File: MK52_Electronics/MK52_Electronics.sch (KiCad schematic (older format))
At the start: 21 parts, among them J1 Processor, J2 KBD Columns, J3 KBD Rows, Q1 BS250, Q2 2N7000, Q3 2N7000, SW1 POWER, U1 4040, U2 4051, U3 4051

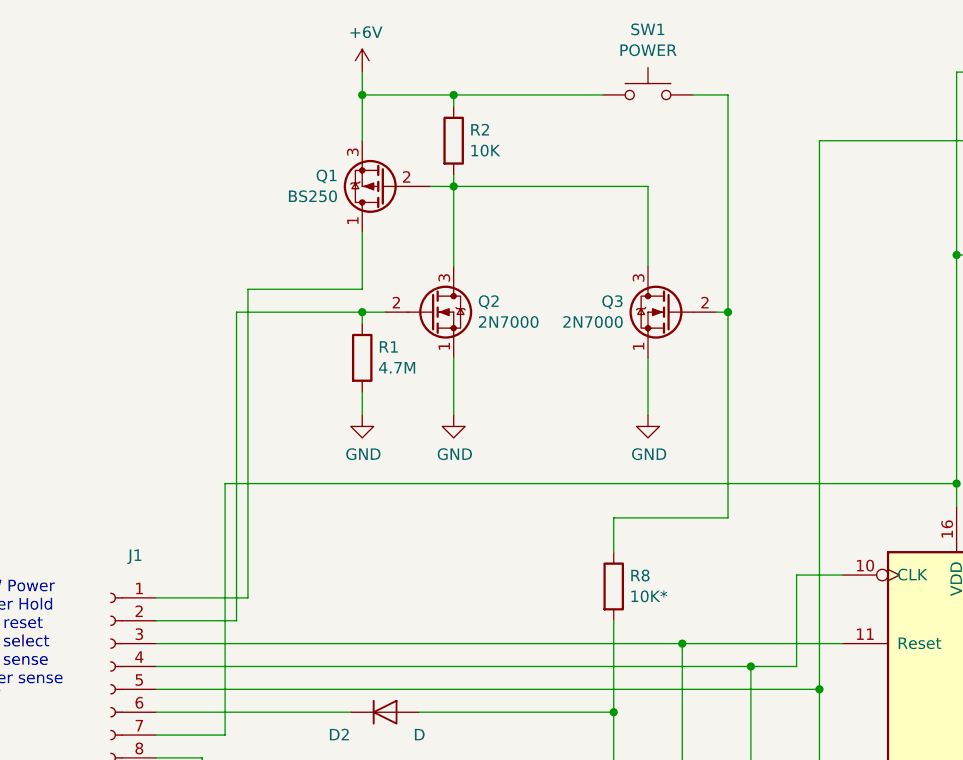
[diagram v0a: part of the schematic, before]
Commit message: Updated gate resistors
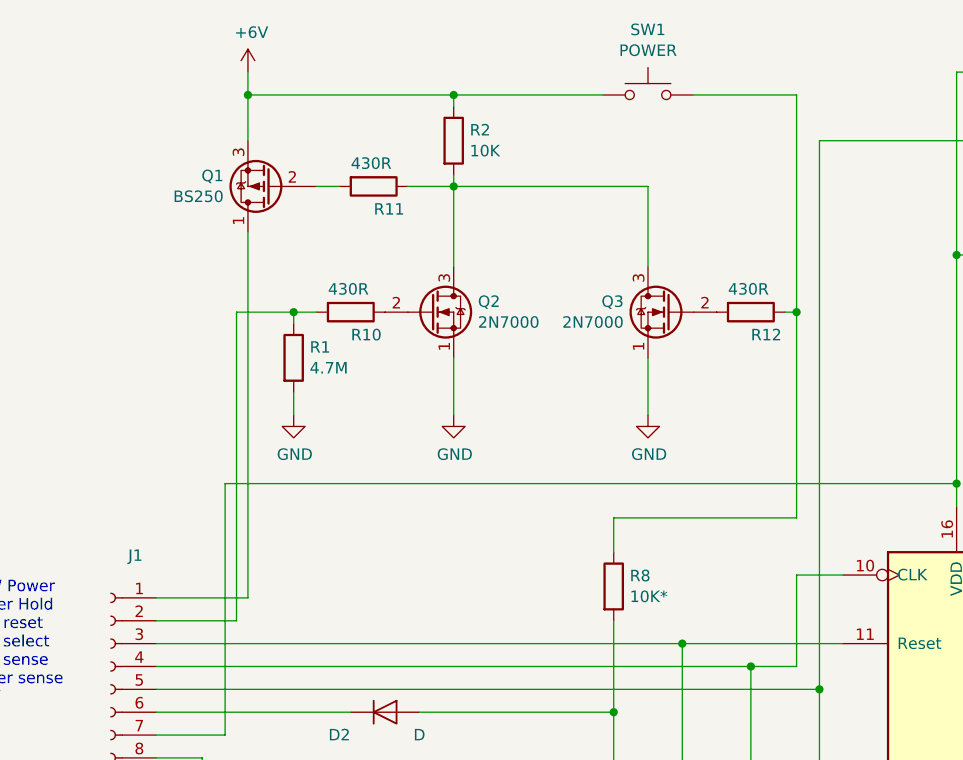
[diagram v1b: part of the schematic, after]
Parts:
- added R10, R11, R12: 430R, symbol Device:R
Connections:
- net at Q2.3 (D), Q3.3 (D), R2.2: now also R11.1; no longer Q1.2 (G)
- net at J1.2 (Pin_2), R1.1: now also R10.2; no longer Q2.2 (G)
- net at R8.1, SW1.2: now also R12.1; no longer Q3.2 (G)
- new net: Q1.2 (G), R11.2
- new net: Q2.2 (G), R10.1
- new net: Q3.2 (G), R12.2
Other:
- moved on the sheet: Q1, R1
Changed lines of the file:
@@
 EESchema Schematic File Version 4
+LIBS:MK52_Electronics-cache
 EELAYER 29 0
 EELAYER END
@@
 L Transistor_FET:BS250 Q1
 U 1 1 5FE6E4D4
-P 3900 1300
-F 0 "Q1" H 4106 1254 50  0000 L CNN
-F 1 "BS250" H 4106 1345 50  0000 L CNN
-F 2 "Package_TO_SOT_THT:TO-92_Inline" H 4100 1225 50  0001 L CIN
-F 3 "http://www.vishay.com/docs/70209/70209.pdf" H 3900 1300 50  0001 L CNN
-	1    3900 1300
+P 3400 1300
+F 0 "Q1" H 3606 1254 50  0000 L CNN
+F 1 "BS250" H 3606 1345 50  0000 L CNN
+F 2 "Package_TO_SOT_THT:TO-92_Inline" H 3600 1225 50  0001 L CIN
+F 3 "http://www.vishay.com/docs/70209/70209.pdf" H 3400 1300 50  0001 L CNN
+	1    3400 1300
 	-1   0    0    1
 $EndComp
@@
 L power:+6V #PWR02
 U 1 1 5FE6EF69
-P 3800 800
-F 0 "#PWR02" H 3800 650 50  0001 C CNN
-F 1 "+6V" H 3815 973 50  0000 C CNN
-F 2 "" H 3800 800 50  0001 C CNN
-F 3 "" H 3800 800 50  0001 C CNN
-	1    3800 800
-	1    0    0    -1
-$EndComp
-Wire Wire Line
-	3800 800  3800 900
+P 3300 800
+F 0 "#PWR02" H 3300 650 50  0001 C CNN
+F 1 "+6V" H 3315 973 50  0000 C CNN
+F 2 "" H 3300 800 50  0001 C CNN
+F 3 "" H 3300 800 50  0001 C CNN
+	1    3300 800
+	1    0    0    -1
+$EndComp
 $Comp
 L Device:R R2
@@
 $EndComp
 Wire Wire Line
-	4100 1300 4200 1300
-Wire Wire Line
 	4200 1300 4200 1250
 Wire Wire Line
-	3800 900  4200 900
-Wire Wire Line
 	4200 900  4200 950
-Connection ~ 3800 900
-Wire Wire Line
-	3800 900  3800 1100
-Wire Wire Line
-	3800 1750 3800 1500
 Text Notes 1950 3650 0    50   ~ 0
 1 - RAW Power\n2 - Power Hold\n3 - KBD reset\n4 - KBD select\n5 - KBD sense\n6 - Power sense\n7 - 3.3V\n8 - GND
@@
 L Device:R R1
 U 1 1 5FE77DA3
-P 3800 2050
-F 0 "R1" H 3870 2096 50  0000 L CNN
-F 1 "4.7M" H 3870 2005 50  0000 L CNN
-F 2 "" V 3730 2050 50  0001 C CNN
-F 3 "~" H 3800 2050 50  0001 C CNN
-	1    3800 2050
+P 3500 2050
+F 0 "R1" H 3570 2096 50  0000 L CNN
+F 1 "4.7M" H 3570 2005 50  0000 L CNN
+F 2 "" V 3430 2050 50  0001 C CNN
+F 3 "~" H 3500 2050 50  0001 C CNN
+	1    3500 2050
 	1    0    0    -1
 $EndComp
 Wire Wire Line
 	4200 1300 4200 1650
-Wire Wire Line
-	3300 1750 3800 1750
 $Comp
 L power:GND #PWR06
@@
 	1    0    0    -1
 $EndComp
-Wire Wire Line
-	3250 1850 3800 1850
 $Comp
 L power:GND #PWR03
 U 1 1 5FE8927B
-P 3800 2300
-F 0 "#PWR03" H 3800 2050 50  0001 C CNN
-F 1 "GND" H 3805 2127 50  0000 C CNN
-F 2 "" H 3800 2300 50  0001 C CNN
-F 3 "" H 3800 2300 50  0001 C CNN
-	1    3800 2300
+P 3500 2300
+F 0 "#PWR03" H 3500 2050 50  0001 C CNN
+F 1 "GND" H 3505 2127 50  0000 C CNN
+F 2 "" H 3500 2300 50  0001 C CNN
+F 3 "" H 3500 2300 50  0001 C CNN
+	1    3500 2300
 	1    0    0    -1
 $EndComp
 Wire Wire Line
 	4200 2050 4200 2300
-Wire Wire Line
-	3800 2200 3800 2300
-Wire Wire Line
-	3800 1850 3800 1900
-Connection ~ 3800 1850
-Wire Wire Line
-	3800 1850 3900 1850
 $Comp
 L Transistor_FET:2N7000 Q3
@@
 	2900 3100 3300 3100
 Wire Wire Line
-	3300 1750 3300 3100
-Wire Wire Line
 	2900 3200 3250 3200
 Wire Wire Line
@@
 Wire Wire Line
 	2900 3600 3750 3600
-Wire Wire Line
-	5400 2750 5400 1850
-Wire Wire Line
-	5400 1850 5350 1850
 $Comp
 L Switch:SW_Push SW1
@@
 	1    0    0    -1
 $EndComp
-Connection ~ 5400 1850
 Wire Wire Line
 	4900 4150 4900 4300
@@
 Wire Wire Line
 	4900 2900 4900 2750
-Wire Wire Line
-	4900 2750 5400 2750
 Connection ~ 4900 3600
 Wire Wire Line
@@
 Connection ~ 4200 900
 Wire Wire Line
-	5250 900  5400 900
-Wire Wire Line
-	5400 900  5400 1850
-Wire Wire Line
 	6400 800  6400 1600
 Wire Wire Line
@@
 Wire Wire Line
 	6400 800  8500 800
+$Comp
+L Device:R R11
+U 1 1 6003BE54
+P 3850 1300
+F 0 "R11" V 3950 1300 50  0000 L CNN
+F 1 "430R" V 3750 1200 50  0000 L CNN
+F 2 "" V 3780 1300 50  0001 C CNN
+F 3 "~" H 3850 1300 50  0001 C CNN
+	1    3850 1300
+	0    1    1    0
+$EndComp
+Wire Wire Line
+	3600 1300 3700 1300
+Wire Wire Line
+	4000 1300 4200 1300
+Wire Wire Line
+	3300 1100 3300 900
+Wire Wire Line
+	3300 800  3300 900
+Connection ~ 3300 900
+Wire Wire Line
+	3300 900  4200 900
+Wire Wire Line
+	3300 1500 3300 3100
+Wire Wire Line
+	3500 2200 3500 2300
+$Comp
+L Device:R R10
+U 1 1 60058690
+P 3750 1850
+F 0 "R10" V 3850 1850 50  0000 L CNN
+F 1 "430R" V 3650 1750 50  0000 L CNN
+F 2 "" V 3680 1850 50  0001 C CNN
+F 3 "~" H 3750 1850 50  0001 C CNN
+	1    3750 1850
+	0    1    1    0
+$EndComp
+Wire Wire Line
+	3250 1850 3500 1850
+Wire Wire Line
+	3500 1900 3500 1850
+Connection ~ 3500 1850
+Wire Wire Line
+	3500 1850 3600 1850
+$Comp
+L Device:R R12
+U 1 1 60060935
+P 5500 1850
+F 0 "R12" V 5600 1850 50  0000 L CNN
+F 1 "430R" V 5400 1750 50  0000 L CNN
+F 2 "" V 5430 1850 50  0001 C CNN
+F 3 "~" H 5500 1850 50  0001 C CNN
+	1    5500 1850
+	0    1    1    0
+$EndComp
+Wire Wire Line
+	5700 900  5700 1850
+Wire Wire Line
+	5700 1850 5650 1850
+Wire Wire Line
+	5250 900  5700 900
+Wire Wire Line
+	5700 1850 5700 2750
+Wire Wire Line
+	4900 2750 5700 2750
+Connection ~ 5700 1850
 $EndSCHEMATC
